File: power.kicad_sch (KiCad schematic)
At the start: 30 parts, among them U1 BD9G101G, U2 BD9G101G

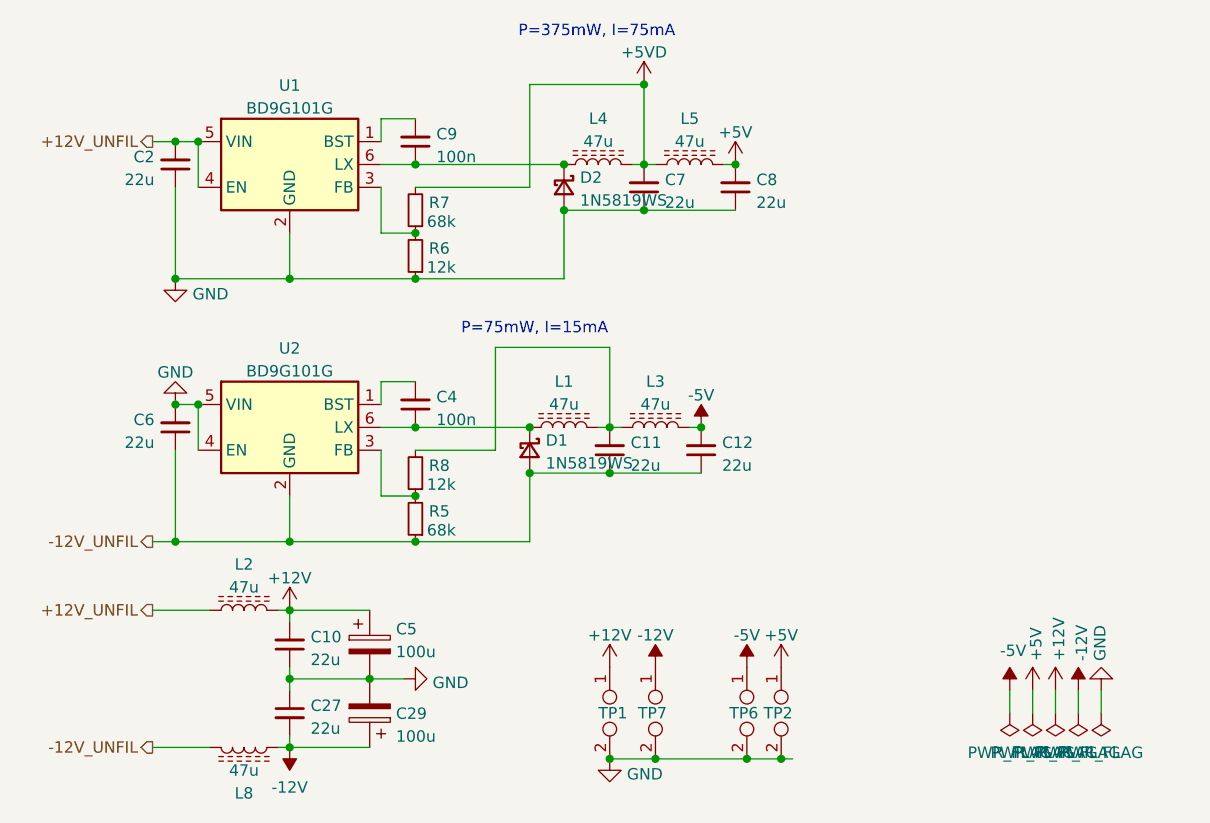
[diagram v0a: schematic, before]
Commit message: Make design more compact
Fitting it on a 100x70mm PCB means it's far cheaper to produce
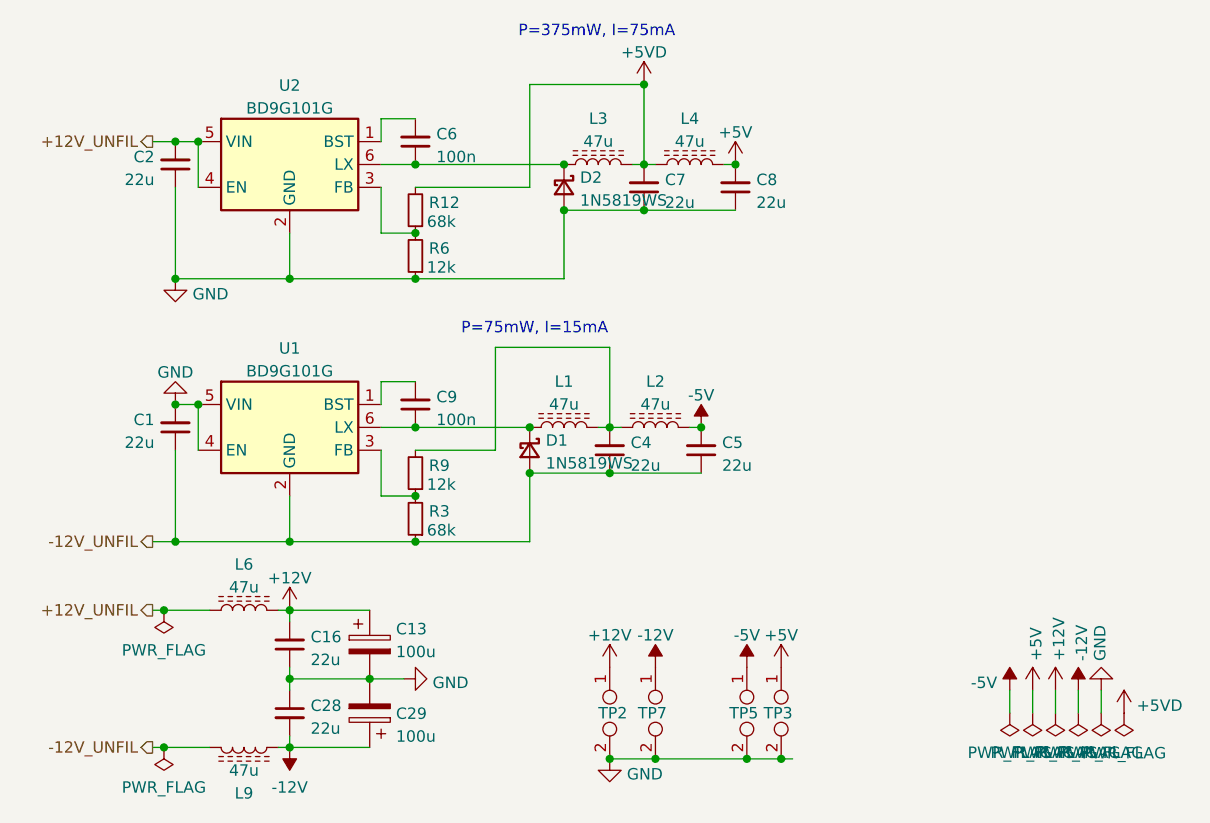
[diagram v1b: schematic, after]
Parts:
- renumbered C6 to C1, C5 to C13, C10 to C16, C27 to C28, C11 to C4, C12 to C5, C9 to C6, C4 to C9, L3 to L2, L4 to L3, L5 to L4, L2 to L6, L8 to L9, R7 to R12, R5 to R3, R8 to R9, TP1 to TP2, TP2 to TP3, TP6 to TP5, U2 to U1, U1 to U2
